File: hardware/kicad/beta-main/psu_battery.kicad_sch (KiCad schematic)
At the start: 0 parts

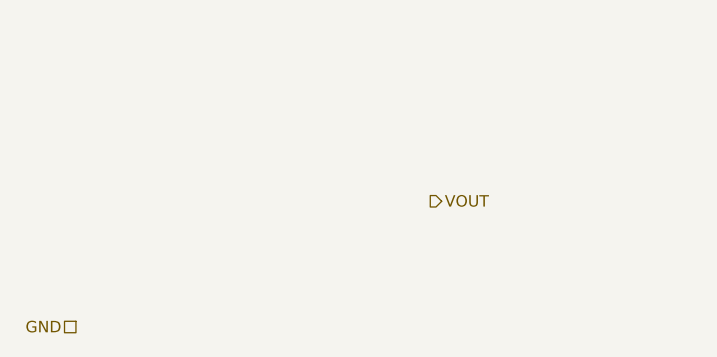
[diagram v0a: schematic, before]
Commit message: 5V and amplifier corrections
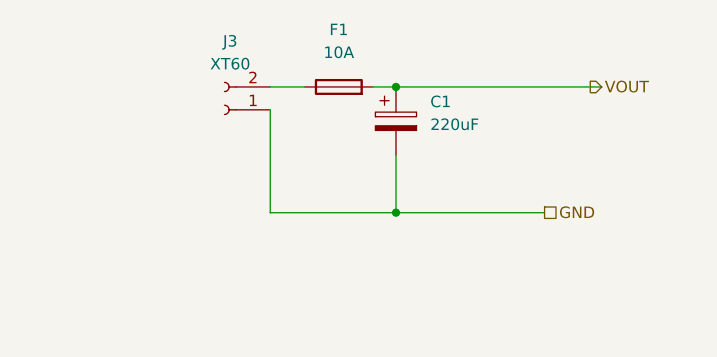
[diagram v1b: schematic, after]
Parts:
- added C1: 220uF, symbol Device:C_Polarized
- added F1: 10A, Fuse:Fuse_1206_3216Metric, symbol Device:Fuse
- added J3: XT60, Connector_AMASS:AMASS_XT60-F_1x02_P7.20mm_Vertical, symbol Connector:Conn_01x02_Socket
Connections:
- net GND: now also C1.2, J3.1 (Pin_1)
- net VOUT: now also C1.1, F1.2
- new net: F1.1, J3.2 (Pin_2)

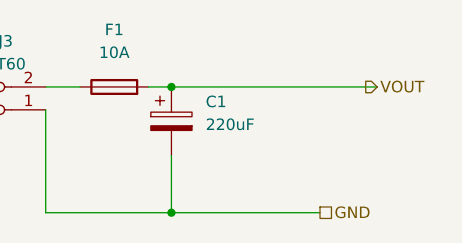
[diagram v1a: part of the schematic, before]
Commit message: Amplifier set for left channel only and god rid of all errors from ERC
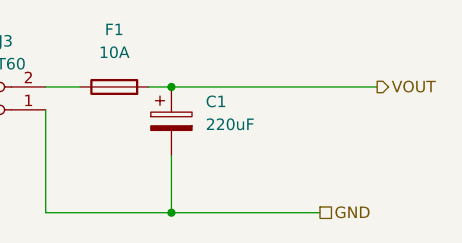
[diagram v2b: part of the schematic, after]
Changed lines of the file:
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@@
 	(hierarchical_label "VOUT"
 		(shape output)
-		(at 123.19 54.61 0)
+		(at 124.46 54.61 0)
 		(effects
 			(font

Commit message: Setup for PCB layout
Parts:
- C1: value 220uF -> 220u; footprint (none) -> Capacitor_SMD:C_1210_3225Metric
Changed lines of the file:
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@@
 			)
 		)
-		(property "Value" "220uF"
+		(property "Value" "220u"
 			(at 105.41 58.8009 0)
 			(effects
@@
 			)
 		)
-		(property "Footprint" ""
+		(property "Footprint" "Capacitor_SMD:C_1210_3225Metric"
 			(at 102.5652 62.23 0)
 			(effects

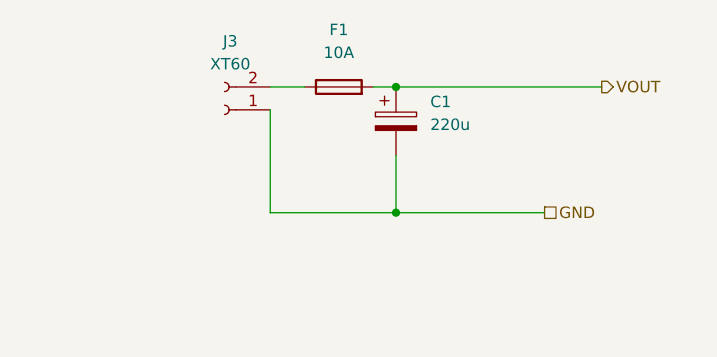
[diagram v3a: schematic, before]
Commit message: remove power symbols from hierarchy and move different subsystems  around
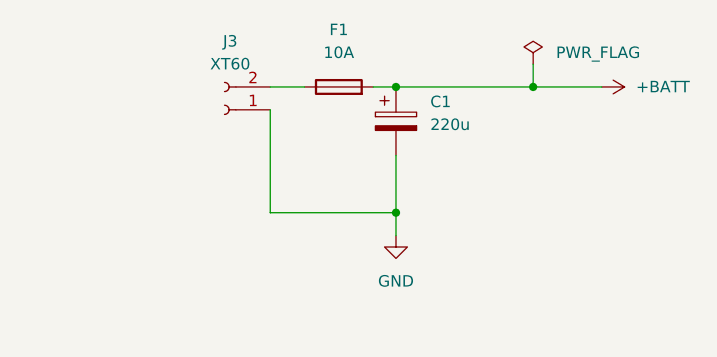
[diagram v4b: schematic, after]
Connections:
- net VOUT renamed +BATT
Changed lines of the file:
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@@
+	)
+	(junction
+		(at 116.84 54.61)
+		(diameter 0)
+		(color 0 0 0 0)
 	)
 	(junction
@@
 	(wire
 		(pts
-			(xy 101.6 68.58) (xy 118.11 68.58)
+			(xy 116.84 52.07) (xy 116.84 54.61)
+		)
+		(stroke
+			(width 0)
+			(type default)
+		)
+	)
+	(wire
+		(pts
+			(xy 116.84 54.61) (xy 124.46 54.61)
 		)
 		(stroke
@@
 	(wire
 		(pts
+			(xy 101.6 71.12) (xy 101.6 68.58)
+		)
+		(stroke
+			(width 0)
+			(type default)
+		)
+	)
+	(wire
+		(pts
 			(xy 99.06 54.61) (xy 101.6 54.61)
 		)
@@
 	(wire
 		(pts
-			(xy 101.6 54.61) (xy 124.46 54.61)
+			(xy 101.6 54.61) (xy 116.84 54.61)
 		)
 		(stroke
@@
 			(width 0)
 			(type default)
-		)
-	)
-	(hierarchical_label "VOUT"
-		(shape output)
-		(at 124.46 54.61 0)
-		(effects
-			(font
-				(size 1.27 1.27)
-			)
-			(justify left)
-		)
-	)
-	(hierarchical_label "GND"
-		(shape passive)
-		(at 118.11 68.58 0)
-		(effects
-			(font
-				(size 1.27 1.27)
-			)
-			(justify left)
 		)
 	)
@@
 	)
 	(symbol
+		(lib_id "power:+BATT")
+		(at 124.46 54.61 270)
+		(unit 1)
+		(exclude_from_sim no)
+		(in_bom yes)
+		(on_board yes)
+		(dnp no)
+		(fields_autoplaced yes)
+		(property "Reference" "#PWR0113"
+			(at 120.65 54.61 0)
+			(effects
+				(font
+					(size 1.27 1.27)
+				)
+				(hide yes)
+			)
+		)
+		(property "Value" "+BATT"
+			(at 128.27 54.6099 90)
+			(effects
+				(font
+					(size 1.27 1.27)
+				)
+				(justify left)
+			)
+		)
+		(property "Footprint" ""
+			(at 124.46 54.61 0)
+			(effects
+				(font
+					(size 1.27 1.27)
+				)
+				(hide yes)
+			)
+		)
+		(property "Datasheet" ""
+			(at 124.46 54.61 0)
+			(effects
+				(font
+					(size 1.27 1.27)
+				)
+				(hide yes)
+			)
+		)
+		(property "Description" "Power symbol creates a global label with name \"+BATT\""
+			(at 124.46 54.61 0)
+			(effects
+				(font
+					(size 1.27 1.27)
+				)
+				(hide yes)
+			)
+		)
+		(pin "1"
+		)
+		(instances
+			(project ""
+				(path "/ec75fd42-4efa-4f32-b57e-76d632cb46f5/a42372fe-a5e6-45a2-9241-7a7c7af267fd/7b048636-3ad8-47aa-9650-ed1a60cc171e"
+					(reference "#PWR0113")
+					(unit 1)
+				)
+			)
+		)
+	)
+	(symbol
+		(lib_id "power:GND")
+		(at 101.6 71.12 0)
+		(unit 1)
+		(exclude_from_sim no)
+		(in_bom yes)
+		(on_board yes)
+		(dnp no)
+		(fields_autoplaced yes)
+		(property "Reference" "#PWR0114"
+			(at 101.6 77.47 0)
+			(effects
+				(font
+					(size 1.27 1.27)
+				)
+				(hide yes)
+			)
+		)
+		(property "Value" "GND"
+			(at 101.6 76.2 0)
+			(effects
+				(font
+					(size 1.27 1.27)
+				)
+			)
+		)
+		(property "Footprint" ""
+			(at 101.6 71.12 0)
+			(effects
+				(font
+					(size 1.27 1.27)
+				)
+				(hide yes)
+			)
+		)
+		(property "Datasheet" ""
+			(at 101.6 71.12 0)
+			(effects
+				(font
+					(size 1.27 1.27)
+				)
+				(hide yes)
+			)
+		)
+		(property "Description" "Power symbol creates a global label with name \"GND\" , ground"
+			(at 101.6 71.12 0)
+			(effects
+				(font
+					(size 1.27 1.27)
+				)
+				(hide yes)
+			)
+		)
+		(pin "1"
+		)
+		(instances
+			(project ""
+				(path "/ec75fd42-4efa-4f32-b57e-76d632cb46f5/a42372fe-a5e6-45a2-9241-7a7c7af267fd/7b048636-3ad8-47aa-9650-ed1a60cc171e"
+					(reference "#PWR0114")
+					(unit 1)
+				)
+			)
+		)
+	)
+	(symbol
 		(lib_id "Device:C_Polarized")
 		(at 101.6 58.42 0)
@@
 					(unit 1)
 				)
+			)
+		)
+	)
+	(symbol
+		(lib_id "power:PWR_FLAG")
+		(at 116.84 52.07 0)
+		(unit 1)
+		(exclude_from_sim no)
+		(in_bom yes)
+		(on_board yes)
+		(dnp no)
+		(fields_autoplaced yes)
+		(property "Reference" "#FLG06"
+			(at 116.84 50.165 0)
+			(effects
+				(font
+					(size 1.27 1.27)
+				)
+				(hide yes)
+			)
+		)
+		(property "Value" "PWR_FLAG"
+			(at 119.38 50.7999 0)
+			(effects
+				(font
+					(size 1.27 1.27)
+				)
+				(justify left)
+			)
+		)
+		(property "Footprint" ""
+			(at 116.84 52.07 0)
+			(effects
+				(font
+					(size 1.27 1.27)
+				)
+				(hide yes)
+			)
+		)
+		(property "Datasheet" "~"
+			(at 116.84 52.07 0)
+			(effects
+				(font
+					(size 1.27 1.27)
+				)
+				(hide yes)
+			)
+		)
+		(property "Description" "Special symbol for telling ERC where power comes from"
+			(at 116.84 52.07 0)
+			(effects
+				(font
+					(size 1.27 1.27)
+				)
+				(hide yes)
+			)
+		)
+		(pin "1"
+		)
+		(instances
+			(project "beta-main"
+				(path "/ec75fd42-4efa-4f32-b57e-76d632cb46f5/a42372fe-a5e6-45a2-9241-7a7c7af267fd/7b048636-3ad8-47aa-9650-ed1a60cc171e"
+					(reference "#FLG06")
+					(unit 1)
+				)

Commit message: Footprints fixed, fuse removed
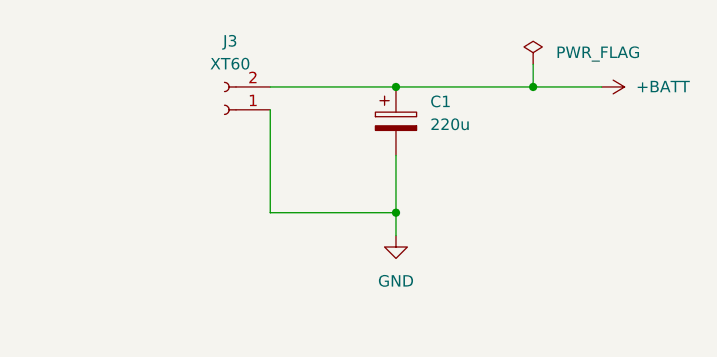
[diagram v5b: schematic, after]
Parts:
- removed F1: 10A, Fuse:Fuse_1206_3216Metric, symbol Device:Fuse
- C1: footprint Capacitor_SMD:C_1210_3225Metric -> Capacitor_SMD:C_0603_1608Metric_Pad1.08x0.95mm_HandSolder
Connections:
- net +BATT: now also J3.2 (Pin_2)
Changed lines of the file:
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@@
 	(wire
 		(pts
-			(xy 87.63 54.61) (xy 91.44 54.61)
+			(xy 87.63 54.61) (xy 101.6 54.61)
 		)
 		(stroke
@@
 		(pts
 			(xy 101.6 71.12) (xy 101.6 68.58)
-		)
-		(stroke
-			(width 0)
-			(type default)
-		)
-	)
-	(wire
-		(pts
-			(xy 99.06 54.61) (xy 101.6 54.61)
 		)
 		(stroke
@@
 			)
 		)
-		(property "Footprint" "Capacitor_SMD:C_1210_3225Metric"
+		(property "Footprint" "Capacitor_SMD:C_0603_1608Metric_Pad1.08x0.95mm_HandSolder"
 			(at 102.5652 62.23 0)
 			(effects
@@
 					(unit 1)
 				)
-			)
-		)
-	)
-	(symbol
-		(lib_id "Device:Fuse")
-		(at 95.25 54.61 90)
-		(unit 1)
-		(exclude_from_sim no)
-		(in_bom yes)
-		(on_board yes)
-		(dnp no)
-		(fields_autoplaced yes)
-		(property "Reference" "F1"
-			(at 95.25 48.26 90)
-			(effects
-				(font
-					(size 1.27 1.27)
-				)
-			)
-		)
-		(property "Value" "10A"
-			(at 95.25 50.8 90)
-			(effects
-				(font
-					(size 1.27 1.27)
-				)
-			)
-		)
-		(property "Footprint" "Fuse:Fuse_1206_3216Metric"
-			(at 95.25 56.388 90)
-			(effects
-				(font
-					(size 1.27 1.27)
-				)
-				(hide yes)
-			)
-		)
-		(property "Datasheet" "~"
-			(at 95.25 54.61 0)
-			(effects
-				(font
-					(size 1.27 1.27)
-				)
-				(hide yes)
-			)
-		)
-		(property "Description" "Fuse"
-			(at 95.25 54.61 0)
-			(effects
-				(font
-					(size 1.27 1.27)
-				)
-				(hide yes)
-			)
-		)
-		(pin "1"
-		)
-		(pin "2"
-		)
-		(instances
-			(project ""
-				(path "/ec75fd42-4efa-4f32-b57e-76d632cb46f5/a42372fe-a5e6-45a2-9241-7a7c7af267fd/7b048636-3ad8-47aa-9650-ed1a60cc171e"
-					(reference "F1")
-					(unit 1)
-				)
